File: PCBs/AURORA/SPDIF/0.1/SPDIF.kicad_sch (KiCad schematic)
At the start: 67 parts, among them J1 Conn_01x02_Male, J10 Conn_01x02_Pin, J11 Conn_01x02_Pin, J12 Conn_01x02_Male, J13 Conn_01x02_Male, J14 Conn_02x10_Odd_Even, J2 Conn_01x02_Male, J3 Conn_01x02_Male, J4 CHANSEL, J5 Conn_01x02_Pin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

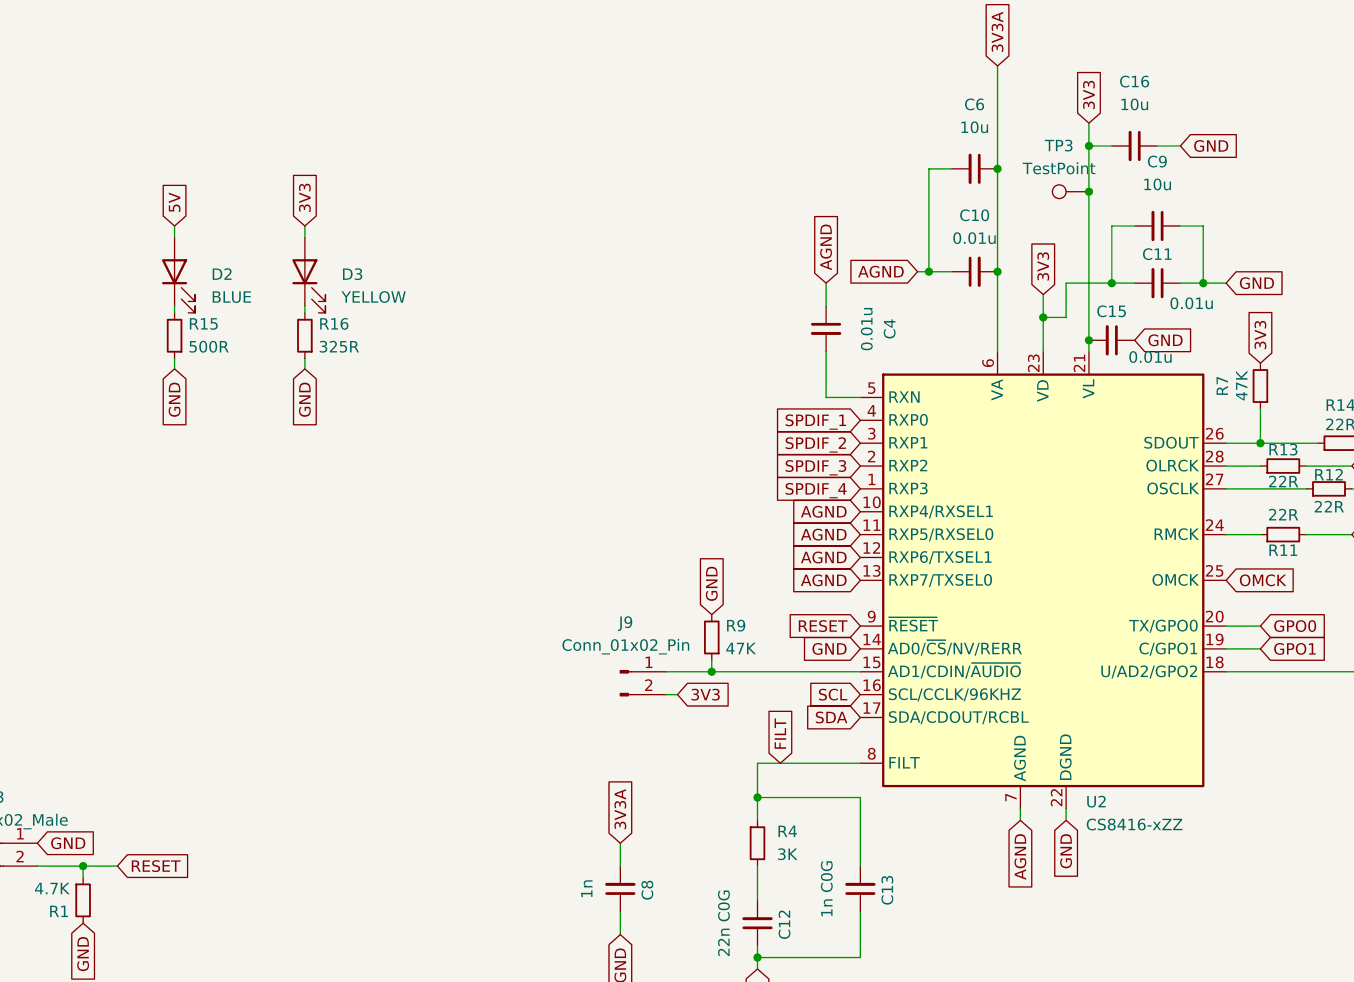
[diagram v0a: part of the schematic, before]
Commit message: Fixing audio issues, leave TRUNC off and at 24 bits
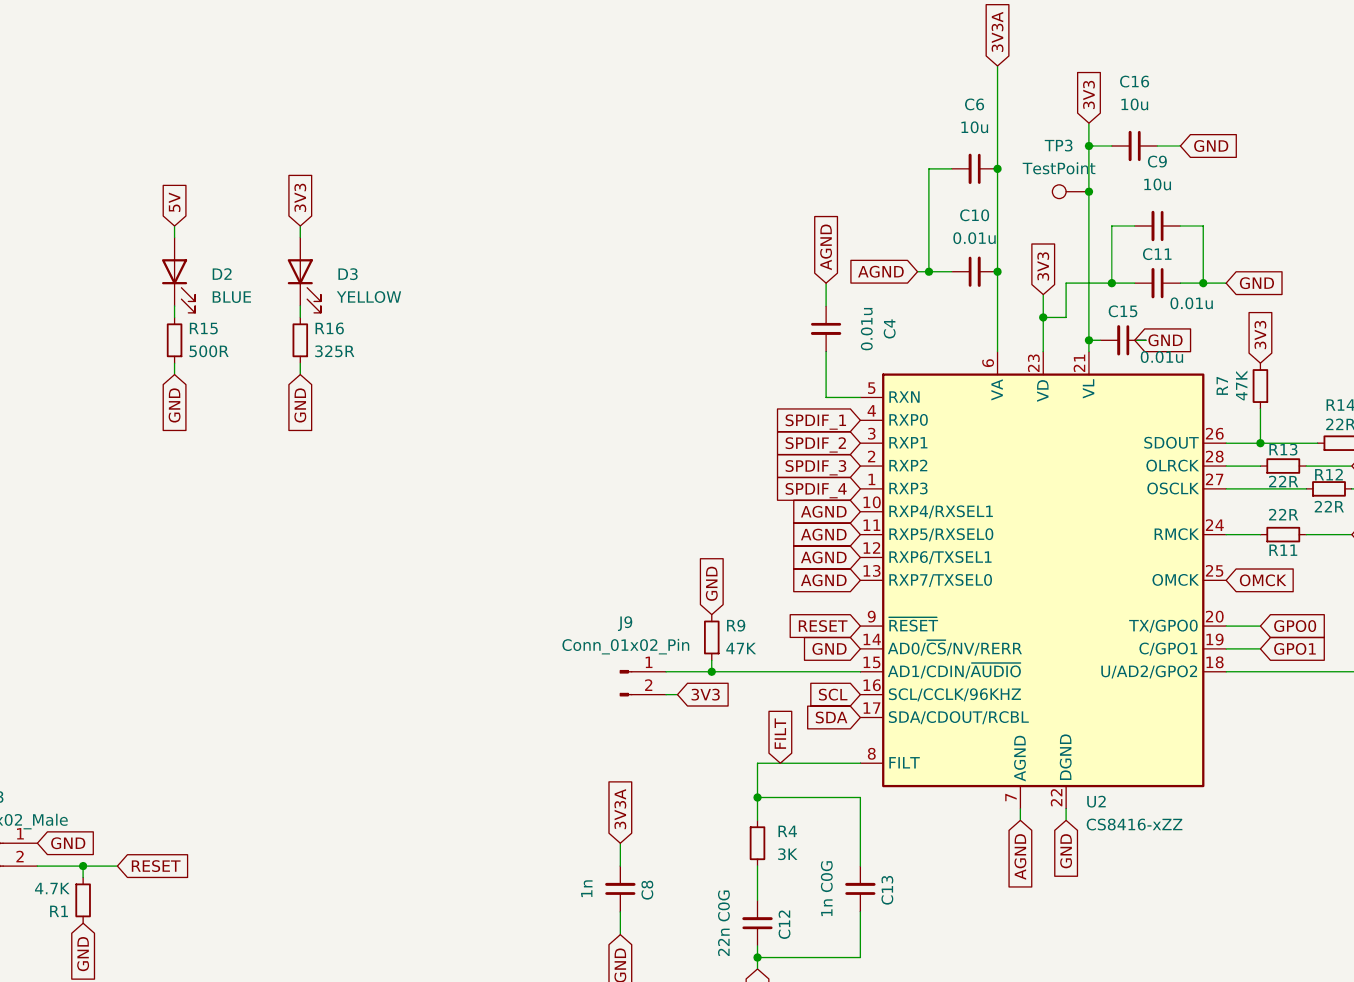
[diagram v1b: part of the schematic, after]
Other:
- moved on the sheet: C15, D3, R15, R16
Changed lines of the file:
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@@
 	)
 	(junction
-		(at 153.67 132.08)
-		(diameter 0)
-		(color 0 0 0 0)
-	)
-	(junction
 		(at 120.65 67.31)
 		(diameter 0)
@@
 	)
 	(junction
+		(at 153.67 132.08)
+		(diameter 0)
+		(color 0 0 0 0)
+	)
+	(junction
 		(at 340.36 100.33)
 		(diameter 0)
@@
 	(wire
 		(pts
-			(xy 52.07 134.112) (xy 52.07 135.255)
+			(xy 52.07 134.62) (xy 52.07 135.89)
 		)
 		(stroke
@@
 	(wire
 		(pts
-			(xy 66.548 120.65) (xy 66.548 119.38)
+			(xy 66.04 120.65) (xy 66.04 119.38)
 		)
 		(stroke
@@
 	(wire
 		(pts
-			(xy 153.67 132.08) (xy 153.67 133.35)
-		)
-		(stroke
-			(width 0)
-			(type default)
-		)
-	)
-	(wire
-		(pts
 			(xy 185.42 77.47) (xy 185.42 78.74)
 		)
@@
 	(wire
 		(pts
+			(xy 146.05 184.15) (xy 146.05 185.42)
+		)
+		(stroke
+			(width 0)
+			(type default)
+		)
+	)
+	(wire
+		(pts
 			(xy 135.89 124.46) (xy 138.43 124.46)
 		)
@@
 	(wire
 		(pts
-			(xy 146.05 185.42) (xy 146.05 184.15)
-		)
-		(stroke
-			(width 0)
-			(type default)
-		)
-	)
-	(wire
-		(pts
 			(xy 172.72 139.7) (xy 172.72 143.51)
 		)
@@
 	(wire
 		(pts
-			(xy 66.548 134.112) (xy 66.548 135.255)
+			(xy 66.04 134.62) (xy 66.04 135.89)
 		)
 		(stroke
@@
 	(wire
 		(pts
+			(xy 154.94 132.08) (xy 153.67 132.08)
+		)
+		(stroke
+			(width 0)
+			(type default)
+		)
+	)
+	(wire
+		(pts
 			(xy 116.84 200.66) (xy 116.84 199.39)
 		)
@@
 	(wire
 		(pts
+			(xy 160.02 132.08) (xy 158.75 132.08)
+		)
+		(stroke
+			(width 0)
+			(type default)
+		)
+	)
+	(wire
+		(pts
 			(xy 148.59 129.54) (xy 148.59 133.35)
 		)
@@
 	(wire
 		(pts
-			(xy 66.548 129.032) (xy 66.548 128.27)
+			(xy 66.04 129.54) (xy 66.04 128.27)
 		)
 		(stroke
@@
 	(wire
 		(pts
-			(xy 52.07 129.032) (xy 52.07 128.27)
+			(xy 52.07 129.54) (xy 52.07 128.27)
 		)
 		(stroke
@@
 	(wire
 		(pts
+			(xy 153.67 132.08) (xy 153.67 133.35)
+		)
+		(stroke
+			(width 0)
+			(type default)
+		)
+	)
+	(wire
+		(pts
 			(xy 151.13 129.54) (xy 148.59 129.54)
 		)
@@
 	(global_label "GND"
 		(shape input)
-		(at 52.07 135.255 270)
+		(at 52.07 135.89 270)
 		(fields_autoplaced yes)
 		(effects
@@
 		)
 		(property "Intersheetrefs" "${INTERSHEET_REFS}"
-			(at 52.07 142.1107 90)
+			(at 52.07 142.7457 90)
 			(effects
 				(font
@@
 	(global_label "GND"
 		(shape input)
-		(at 66.548 135.255 270)
+		(at 66.04 135.89 270)
 		(fields_autoplaced yes)
 		(effects
@@
 		)
 		(property "Intersheetrefs" "${INTERSHEET_REFS}"
-			(at 66.548 142.1107 90)
+			(at 66.04 142.7457 90)
 			(effects
 				(font
@@
 	(global_label "3V3"
 		(shape input)
-		(at 66.548 119.38 90)
+		(at 66.04 119.38 90)
 		(fields_autoplaced yes)
 		(effects
@@
 		)
 		(property "Intersheetrefs" "${INTERSHEET_REFS}"
-			(at 66.548 112.8872 90)
+			(at 66.04 112.8872 90)
 			(effects
 				(font
@@
 	(symbol
 		(lib_id "Device:C_Small")
-		(at 156.21 132.08 270)
+		(at 157.48 132.08 270)
 		(unit 1)
 		(exclude_from_sim no)
@@
 		(dnp no)
 		(property "Reference" "C15"
-			(at 156.21 128.905 90)
+			(at 157.48 128.905 90)
 			(effects
 				(font
@@
 		)
 		(property "Value" "0.01u"
-			(at 160.528 133.985 90)
+			(at 161.798 133.985 90)
 			(effects
 				(font
@@
 		)
 		(property "Footprint" "Capacitor_SMD:C_0805_2012Metric"
-			(at 156.21 132.08 0)
+			(at 157.48 132.08 0)
 			(effects
 				(font
@@
 		)
 		(property "Datasheet" "~"
-			(at 156.21 132.08 0)
+			(at 157.48 132.08 0)
 			(effects
 				(font
@@
 		)
 		(property "Description" "Unpolarized capacitor, small symbol"
-			(at 156.21 132.08 0)
+			(at 157.48 132.08 0)
 			(effects
 				(font
@@
 	(symbol
 		(lib_id "Device:R_Small")
-		(at 66.548 131.572 180)
+		(at 66.04 132.08 180)
 		(unit 1)
 		(exclude_from_sim no)
@@
 		(fields_autoplaced yes)
 		(property "Reference" "R16"
-			(at 68.072 130.302 0)
+			(at 67.564 130.81 0)
 			(effects
 				(font
@@
 		)
 		(property "Value" "325R"
-			(at 68.072 132.842 0)
+			(at 67.564 133.35 0)
 			(effects
 				(font
@@
 		)
 		(property "Footprint" "Resistor_SMD:R_0603_1608Metric_Pad0.98x0.95mm_HandSolder"
-			(at 66.548 131.572 0)
+			(at 66.04 132.08 0)
 			(effects
 				(font
@@
 		)
 		(property "Datasheet" "~"
-			(at 66.548 131.572 0)
+			(at 66.04 132.08 0)
 			(effects
 				(font
@@
 		)
 		(property "Description" ""
-			(at 66.548 131.572 0)
+			(at 66.04 132.08 0)
 			(effects
 				(font
@@
 	(symbol
 		(lib_id "Device:R_Small")
-		(at 52.07 131.572 180)
+		(at 52.07 132.08 180)
 		(unit 1)
 		(exclude_from_sim no)
@@
 		(fields_autoplaced yes)
 		(property "Reference" "R15"
-			(at 53.594 130.302 0)
+			(at 53.594 130.81 0)
 			(effects
 				(font
@@
 		)
 		(property "Value" "500R"
-			(at 53.594 132.842 0)
+			(at 53.594 133.35 0)
 			(effects
 				(font
@@
 		)
 		(property "Footprint" "Resistor_SMD:R_0603_1608Metric_Pad0.98x0.95mm_HandSolder"
-			(at 52.07 131.572 0)
+			(at 52.07 132.08 0)
 			(effects
 				(font
@@
 		)
 		(property "Datasheet" "~"
-			(at 52.07 131.572 0)
+			(at 52.07 132.08 0)
 			(effects
 				(font
@@
 		)
 		(property "Description" ""
-			(at 52.07 131.572 0)
+			(at 52.07 132.08 0)
 			(effects
 				(font
@@
 	(symbol
 		(lib_id "Device:LED")
-		(at 66.548 124.46 90)
+		(at 66.04 124.46 90)
 		(unit 1)
 		(exclude_from_sim no)
@@
 		(fields_autoplaced yes)
 		(property "Reference" "D3"
-			(at 70.612 124.7775 90)
+			(at 70.104 124.7775 90)
 			(effects
 				(font
@@
 		)
 		(property "Value" "YELLOW"
-			(at 70.612 127.3175 90)
+			(at 70.104 127.3175 90)
 			(effects
 				(font
@@
 		)
 		(property "Footprint" "LED_SMD:LED_0805_2012Metric_Pad1.15x1.40mm_HandSolder"
-			(at 66.548 124.46 0)
+			(at 66.04 124.46 0)
 			(effects
 				(font
@@
 		)
 		(property "Datasheet" "~"
-			(at 66.548 124.46 0)
+			(at 66.04 124.46 0)
 			(effects
 				(font
@@
 		)
 		(property "Description" ""
-			(at 66.548 124.46 0)
+			(at 66.04 124.46 0)
 			(effects
 				(font
